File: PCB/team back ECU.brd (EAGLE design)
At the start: 69.5 x 69.8 mm, 12 parts, among them IC2 ICL7663CPA

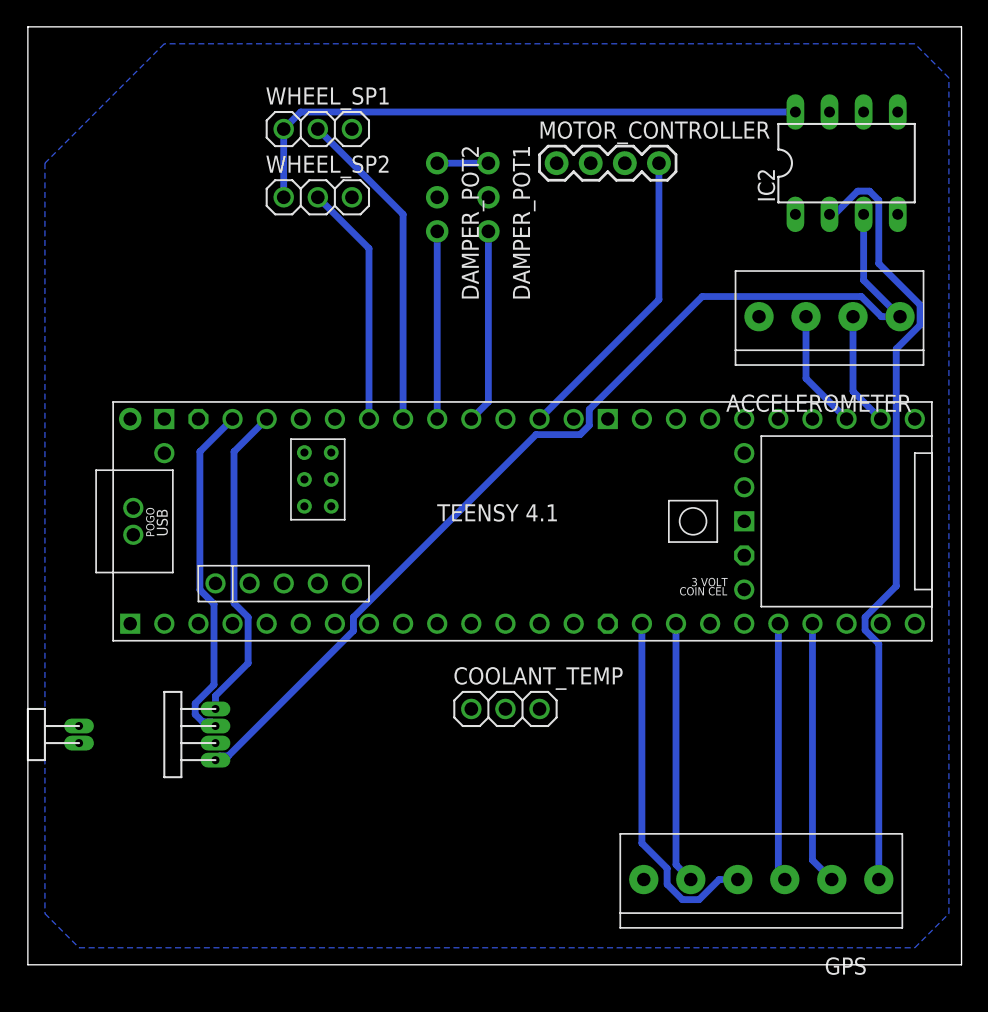
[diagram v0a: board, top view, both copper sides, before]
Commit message: Stress board for Wheat bridge and edits
Created the Wheat bridge board with the different stress gauges in the F-E library. There were some minor edits that the other boards needed as well.
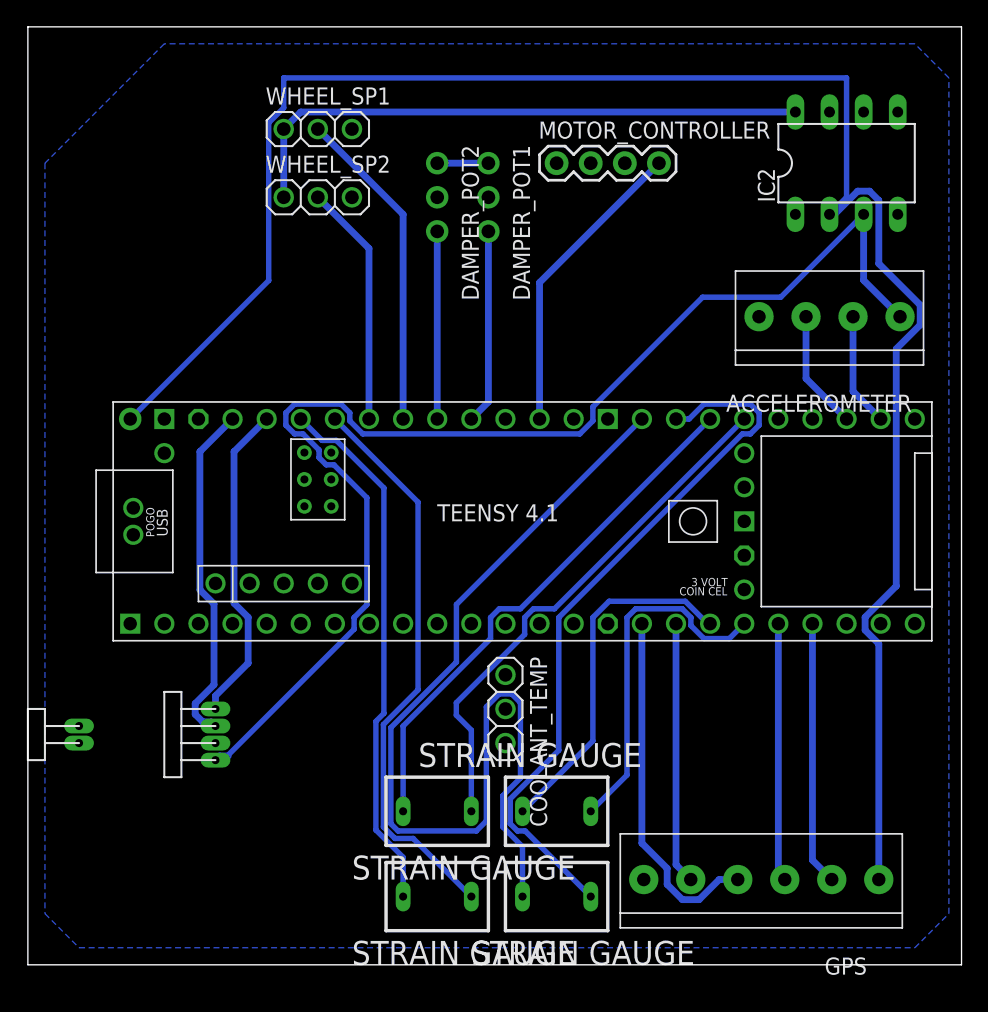
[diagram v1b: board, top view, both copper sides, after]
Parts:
- added U$2, U$3, U$4, U$5: STR_GAUGE, F-E library custom components:STR_GAUGE
- turned COOLANT_TEMP to 270 degrees
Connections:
- new net STR1_H: U$1.21-A7/RX5/BCLK1, U$2.P$1
- new net STR1_L: U$1.20-A6/TX5/LRCLK1, U$2.P$2
- new net STR2_H: U$1.27-A13/SCK1, U$3.P$1
- new net STR2_L: U$1.26-A12/MOSI1, U$3.P$2
- new net STR3_H: U$1.39-A15/CS/OUT1A, U$4.P$1
- new net STR3_L: U$1.38-A14/CS/IN1, U$4.P$2
- new net STR4_H: U$1.41-A17/MISO1, U$5.P$1
- new net STR4_L: U$1.40-A16/CS1, U$5.P$2
- net 5V: now also U$1.VIN
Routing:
- net 5V: track 58.6 -> 141.4 mm
- net STR4_H: track 0.00 -> 72.8 mm
- net STR4_L: track 0.00 -> 53.8 mm
- net STR1_L: track 0.00 -> 42.7 mm
- net STR1_H: track 0.00 -> 39.8 mm
- net STR3_H: track 0.00 -> 39.6 mm
- net STR3_L: track 0.00 -> 39.5 mm
- net STR2_L: track 0.00 -> 26.5 mm
- net STR2_H: track 0.00 -> 26.3 mm
- net 3.3V: track 75.9 -> 95.8 mm
